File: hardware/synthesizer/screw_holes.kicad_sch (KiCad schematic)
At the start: 4 parts

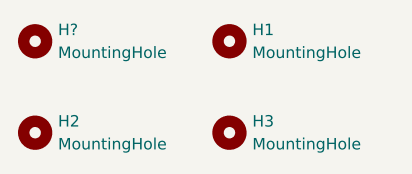
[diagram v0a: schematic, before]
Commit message: finish ethernet jack
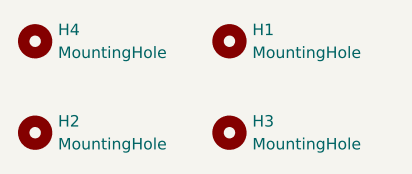
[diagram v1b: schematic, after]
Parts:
- gave numbers to parts that had none: 1
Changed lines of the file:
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@@
 		(dnp no)
 		(fields_autoplaced yes)
-		(property "Reference" "H?"
+		(property "Reference" "H4"
 			(at 121.92 76.1999 0)
 			(effects
@@
 			(project ""
 				(path "/f8740766-88d0-4c4d-b661-742f36f22c7b/b2b162f9-d354-4f12-b96e-cc775f5e80e4"
-					(reference "H?")
+					(reference "H4")
 					(unit 1)
 				)

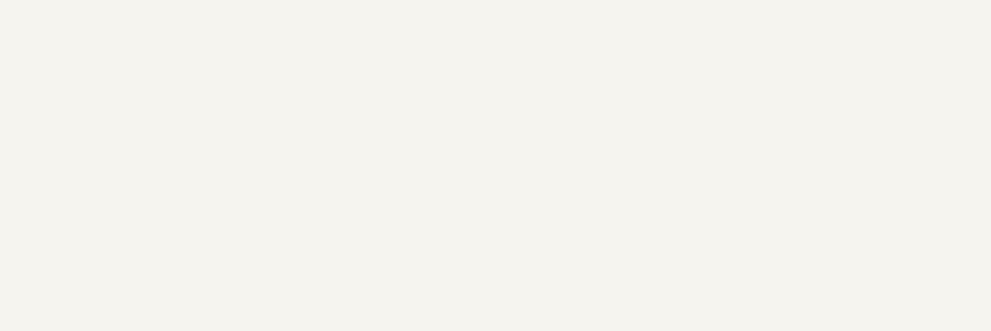
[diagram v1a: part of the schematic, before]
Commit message: add logo to every sheet
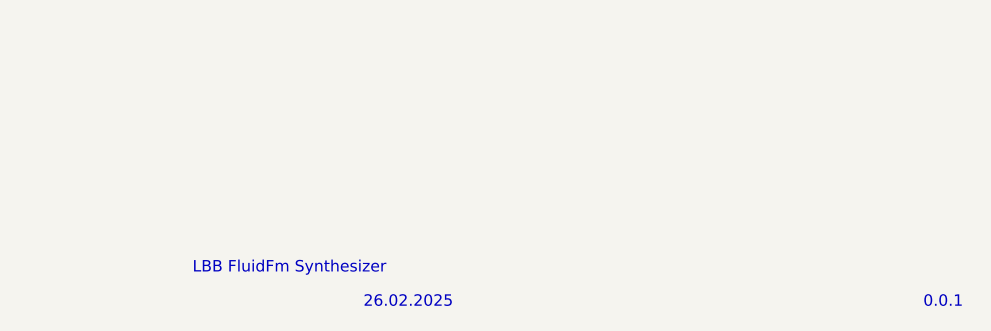
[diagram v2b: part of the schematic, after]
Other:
- note added: "0.0.1"
- note added: "26.02.2025"
- note added: "LBB FluidFm Synthesizer"

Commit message: improved pcb design
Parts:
- H1, H2, H3, H4: footprint (none) -> MountingHole:MountingHole_2.2mm_M2_Pad
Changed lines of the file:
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@@
 			)
 		)
-		(property "Footprint" ""
+		(property "Footprint" "MountingHole:MountingHole_2.2mm_M2_Pad"
 			(at 119.38 87.63 0)
 			(effects
@@
 			)
 		)
-		(property "Footprint" ""
+		(property "Footprint" "MountingHole:MountingHole_2.2mm_M2_Pad"
 			(at 140.97 77.47 0)
 			(effects
@@
 			)
 		)
-		(property "Footprint" ""
+		(property "Footprint" "MountingHole:MountingHole_2.2mm_M2_Pad"
 			(at 119.38 77.47 0)
 			(effects
@@
 			)
 		)
-		(property "Footprint" ""
+		(property "Footprint" "MountingHole:MountingHole_2.2mm_M2_Pad"
 			(at 140.97 87.63 0)
 			(effects
